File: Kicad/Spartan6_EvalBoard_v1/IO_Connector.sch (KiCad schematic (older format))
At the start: 0 parts

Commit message: Schematic almost done
Schematic almost done, just to connect connector to FPGA
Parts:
- added C? (x4): 10u, ~, symbol C
- added C? (x4): 1u, ~, symbol C
- added C? (x4): 100n, ~, symbol C
- added D?: DIODESCH, ~, symbol DIODESCH
- added J? (x2): CON2X50, MODULE, symbol CON2X50
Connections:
- net labels added: +1.2V, +3.3V, +5V, GND, IO1, IO10, IO11, IO12, IO13, IO14, IO15, IO16, IO17, IO18, IO19, IO2, IO20, IO21, IO22, IO23, IO24, IO25, IO26, IO27, IO28, IO29, IO3, IO30, IO31, IO32, IO33, IO34, IO35, IO36, IO37, IO38, IO39, IO4, IO40, IO41, IO42, IO43, IO44, IO45, IO46, IO47, IO48, IO49, IO5, IO50, IO51, IO52, IO53, IO54, IO55, IO56, IO57, IO58, IO59, IO6, IO60, IO61, IO62, IO63, IO64, IO65, IO66, IO67, IO68, IO69, IO7, IO70, IO8, IO9, VCC
- wire segments 0 -> 179

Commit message: Schematic and netllist created
The correct fpga connection to connector will have to be carried out.
Some more footprints need to be created.
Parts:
- gave numbers to parts that had none: 14
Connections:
- net labels added: 1.2V, 3.3V, 5V, IO[1..70], VCC_OUT
- net labels removed: +1.2V, +3.3V, +5V
- wire segments 179 -> 134
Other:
- moved on the sheet: C201, C202, C203, C204, C205, C206, C207, C208, C209, C210, C211, C212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

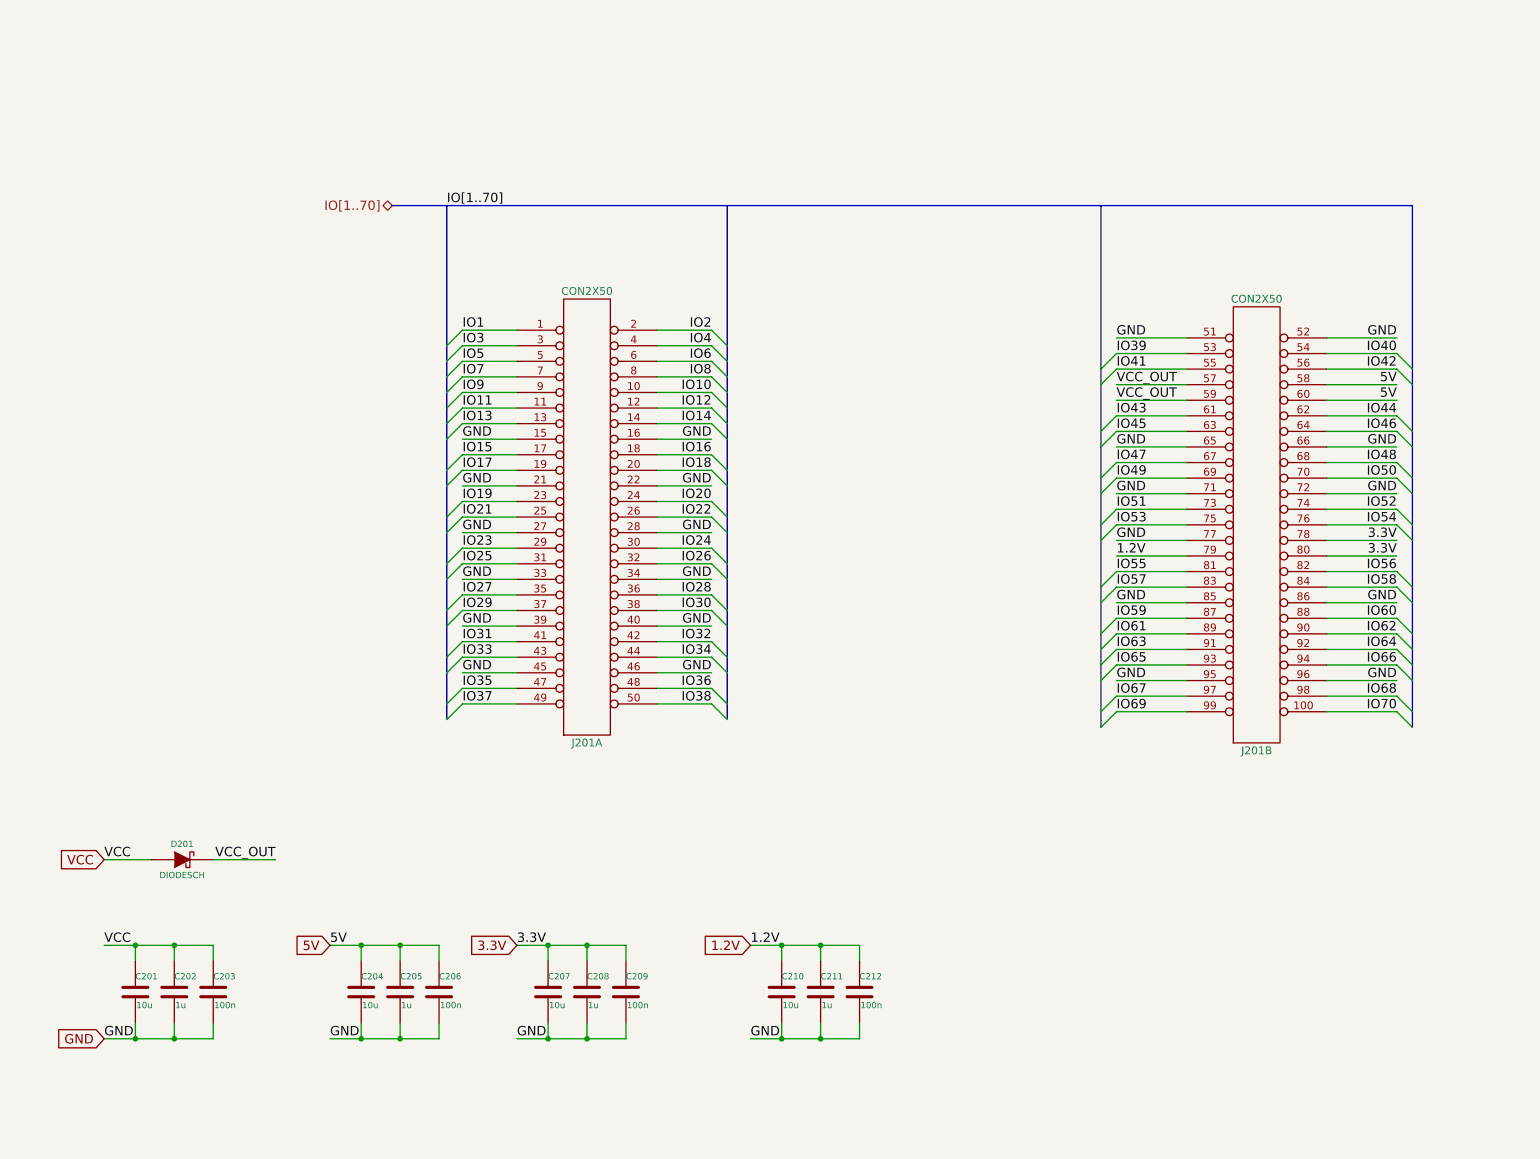
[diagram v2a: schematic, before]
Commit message: Schematic completed, layout starte
Schematic completed, layout starte
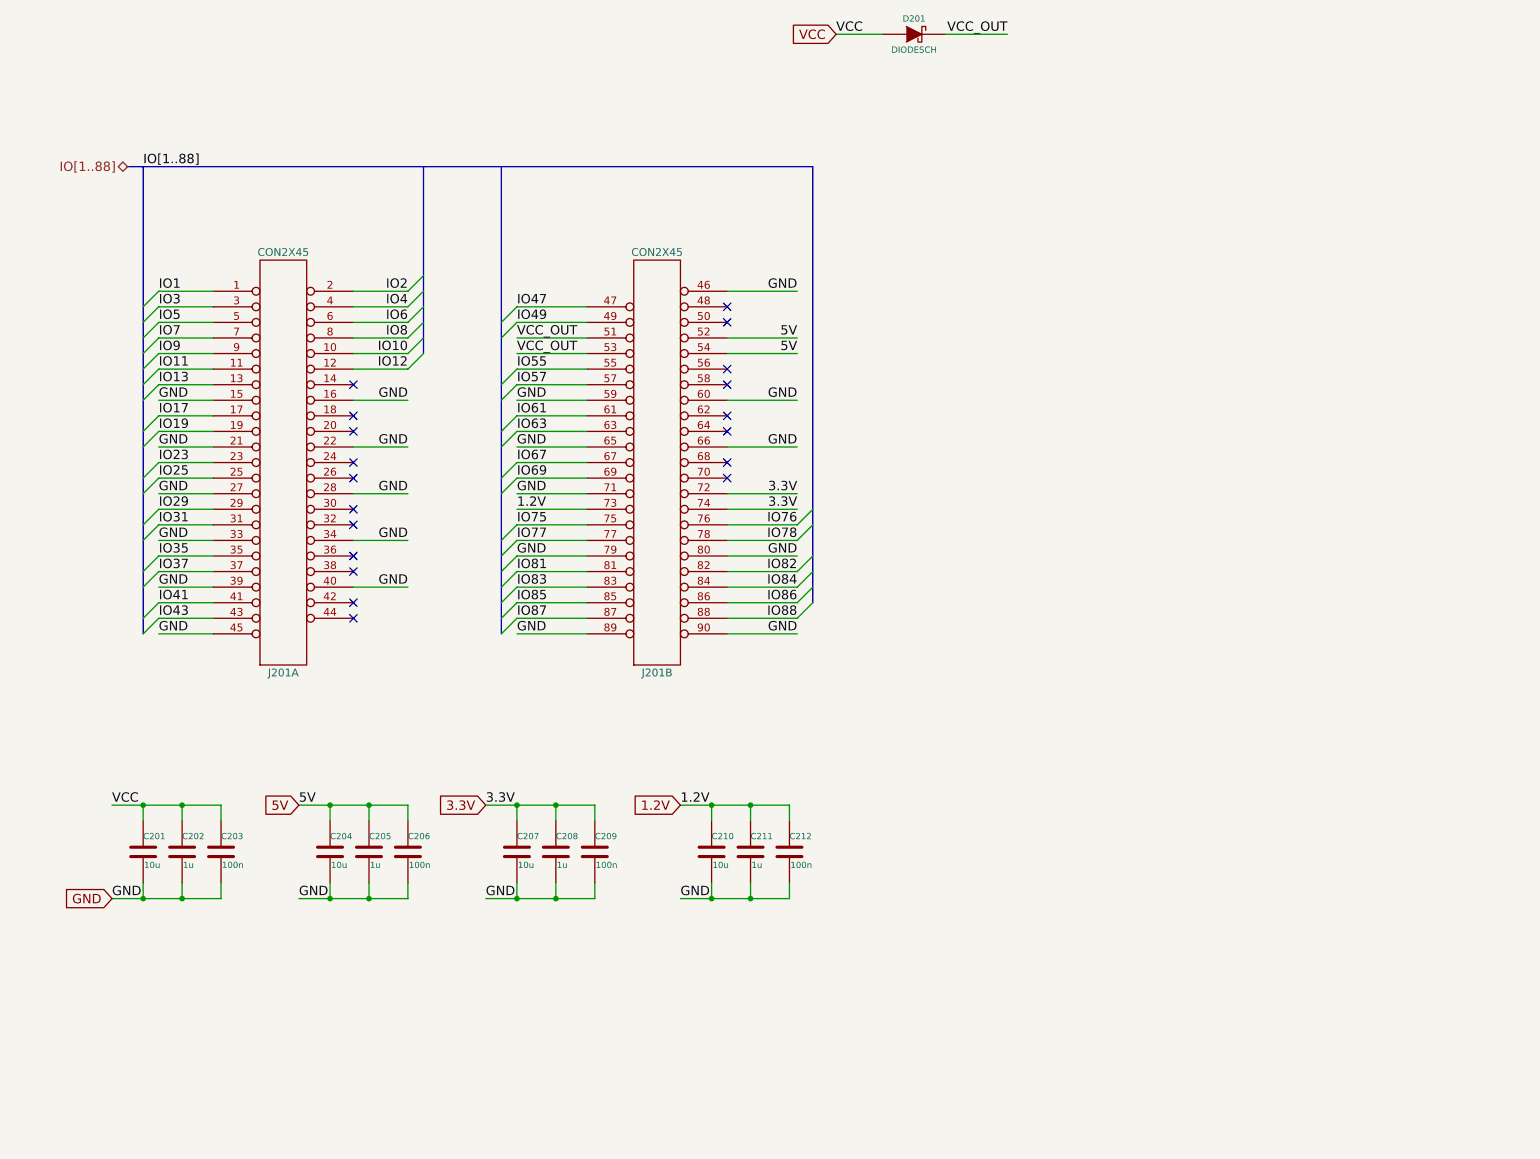
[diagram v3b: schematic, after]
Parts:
- removed J201: CON2X50, MODULE, symbol CON2X50
- added J201: CON2X45, MODULE, symbol CON2X45
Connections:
- net 1.2V: now also J201.73
- net 3.3V: now also J201.72, J201.74
- net 5V: now also J201.52, J201.54
- net GND: now also J201.15, J201.16, J201.21, J201.22, J201.27, J201.28, J201.33, J201.34, J201.39, J201.40, J201.45, J201.46, J201.59, J201.60, J201.65, J201.66, J201.71, J201.79, J201.80, J201.89, J201.90
- net IO1: now also J201.1
- net IO10: now also J201.10
- net IO11: now also J201.11
- net IO12: now also J201.12
- net IO13: now also J201.13
- net IO17: now also J201.17
- net IO19: now also J201.19
- net IO2: now also J201.2
- net IO23: now also J201.23
- net IO25: now also J201.25
- net IO29: now also J201.29
- net IO3: now also J201.3
- net IO31: now also J201.31
- net IO35: now also J201.35
- net IO37: now also J201.37
- net IO4: now also J201.4
- net IO41: now also J201.41
- net IO43: now also J201.43
- net IO47: now also J201.47
- net IO49: now also J201.49
- net IO5: now also J201.5
- net IO55: now also J201.55
- net IO57: now also J201.57
- net IO6: now also J201.6
- net IO61: now also J201.61
- net IO63: now also J201.63
- net IO67: now also J201.67
- net IO69: now also J201.69
- net IO7: now also J201.7
- net IO8: now also J201.8
- net IO9: now also J201.9
- net VCC_OUT: now also J201.51, J201.53
- new net IO75: J201.75
- new net IO76: J201.76
- new net IO77: J201.77
- new net IO78: J201.78
- new net IO81: J201.81
- new net IO82: J201.82
- new net IO83: J201.83
- new net IO84: J201.84
- new net IO85: J201.85
- new net IO86: J201.86
- new net IO87: J201.87
- new net IO88: J201.88
- no-connect marks 0 -> 19
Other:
- moved on the sheet: C201, C202, C203, C204, C205, C206, C207, C208, C209, C210, C211, C212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

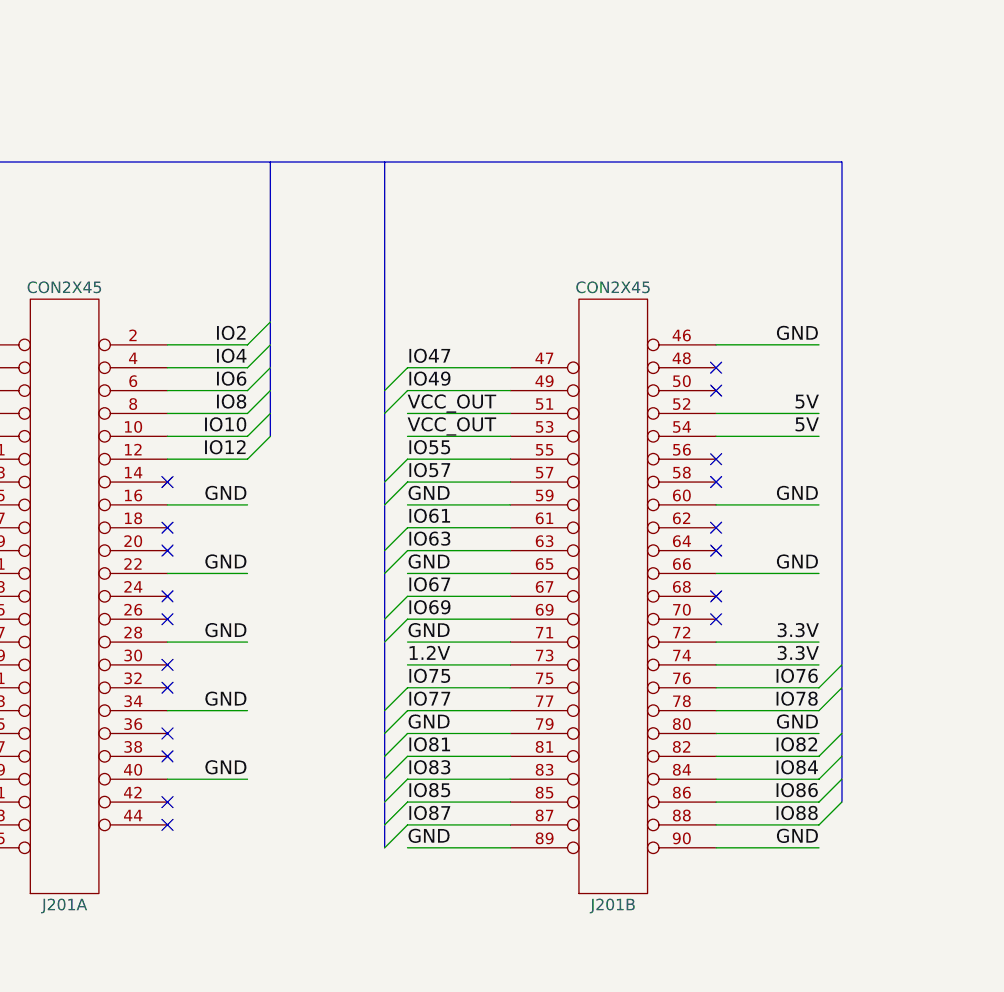
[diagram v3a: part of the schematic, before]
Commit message: BZR - Layout half done
Using LaunchPad Kicad
Layout more than half completed
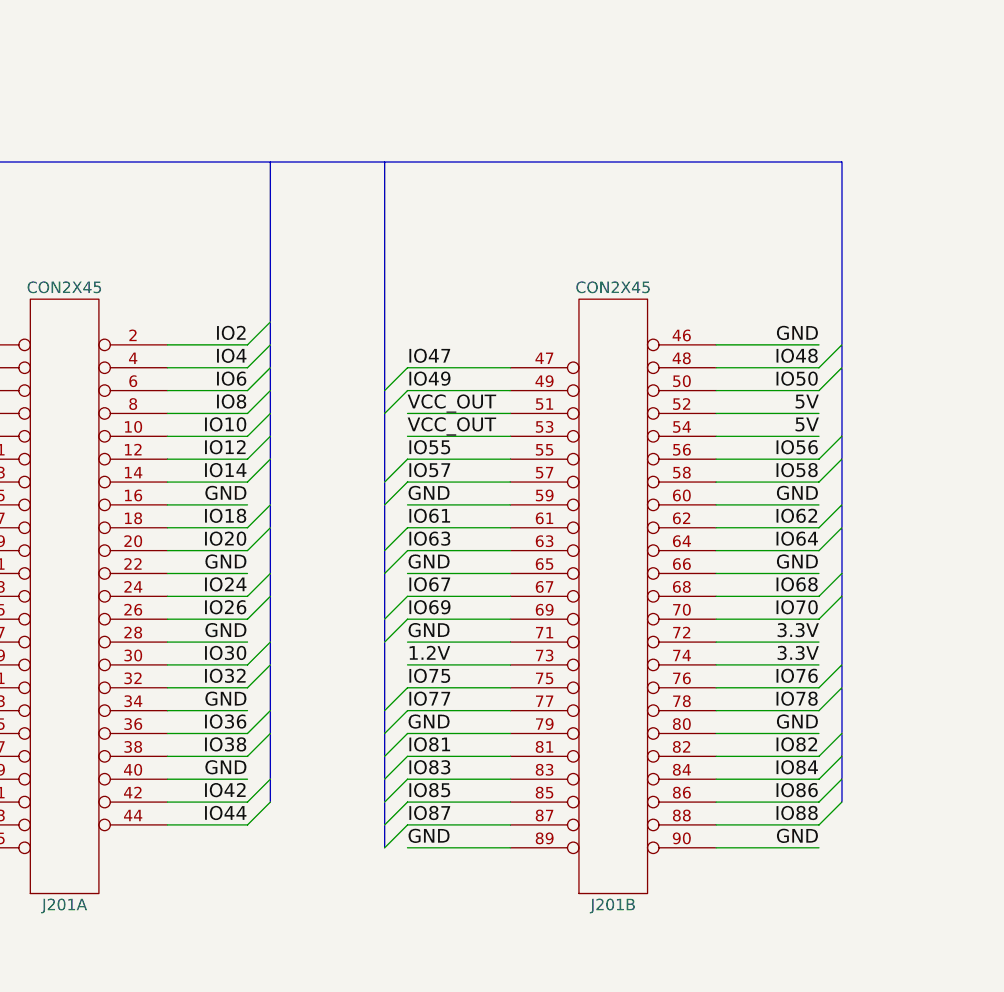
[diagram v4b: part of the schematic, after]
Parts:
- C201, C204, C207, C210: footprint ~ -> Capacitors_SMD.pretty:C_0603
- C202, C203, C205, C206, C208, C209, C211, C212: footprint ~ -> Capacitors_SMD.pretty:C_0402
- D201: footprint ~ -> Eric.mod:SOD-123FL
- J201: footprint MODULE -> Eric.mod:CON45X2
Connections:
- net IO48: now reaches J201.48
- net IO50: now reaches J201.50
- net IO56: now reaches J201.56
- net IO58: now reaches J201.58
- net IO62: now reaches J201.62
- net IO64: now reaches J201.64
- net IO68: now reaches J201.68
- net IO70: now reaches J201.70
- net IO14: now reaches J201.14
- net IO18: now reaches J201.18
- net IO20: now reaches J201.20
- net IO24: now reaches J201.24
- net IO26: now reaches J201.26
- net IO30: now reaches J201.30
- net IO32: now reaches J201.32
- net IO36: now reaches J201.36
- net IO38: now reaches J201.38
- net IO42: now reaches J201.42
- net IO44: now reaches J201.44
- no-connect marks 19 -> 0
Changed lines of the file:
@@
 LIBS:Eric
 LIBS:Spartan6_EvalBoard_v1-cache
-EELAYER 27 0
+EELAYER 25 0
 EELAYER END
 $Descr A4 11693 8268
@@
 F 0 "C201" H 1200 6450 40  0000 L CNN
 F 1 "10u" H 1206 6265 40  0000 L CNN
-F 2 "~" H 1238 6200 30  0000 C CNN
+F 2 "Capacitors_SMD.pretty:C_0603" H 1238 6200 30  0001 C CNN
 F 3 "~" H 1200 6350 60  0000 C CNN
 	1    1200 6350
@@
 F 0 "C202" H 1450 6450 40  0000 L CNN
 F 1 "1u" H 1456 6265 40  0000 L CNN
-F 2 "~" H 1488 6200 30  0000 C CNN
+F 2 "Capacitors_SMD.pretty:C_0402" H 1488 6200 30  0001 C CNN
 F 3 "~" H 1450 6350 60  0000 C CNN
 	1    1450 6350
@@
 F 0 "C203" H 1700 6450 40  0000 L CNN
 F 1 "100n" H 1706 6265 40  0000 L CNN
-F 2 "~" H 1738 6200 30  0000 C CNN
+F 2 "Capacitors_SMD.pretty:C_0402" H 1738 6200 30  0001 C CNN
 F 3 "~" H 1700 6350 60  0000 C CNN
 	1    1700 6350
@@
 F 0 "C204" H 2400 6450 40  0000 L CNN
 F 1 "10u" H 2406 6265 40  0000 L CNN
-F 2 "~" H 2438 6200 30  0000 C CNN
+F 2 "Capacitors_SMD.pretty:C_0603" H 2438 6200 30  0001 C CNN
 F 3 "~" H 2400 6350 60  0000 C CNN
 	1    2400 6350
@@
 F 0 "C205" H 2650 6450 40  0000 L CNN
 F 1 "1u" H 2656 6265 40  0000 L CNN
-F 2 "~" H 2688 6200 30  0000 C CNN
+F 2 "Capacitors_SMD.pretty:C_0402" H 2688 6200 30  0001 C CNN
 F 3 "~" H 2650 6350 60  0000 C CNN
 	1    2650 6350
@@
 F 0 "C206" H 2900 6450 40  0000 L CNN
 F 1 "100n" H 2906 6265 40  0000 L CNN
-F 2 "~" H 2938 6200 30  0000 C CNN
+F 2 "Capacitors_SMD.pretty:C_0402" H 2938 6200 30  0001 C CNN
 F 3 "~" H 2900 6350 60  0000 C CNN
 	1    2900 6350
@@
 F 0 "C207" H 3600 6450 40  0000 L CNN
 F 1 "10u" H 3606 6265 40  0000 L CNN
-F 2 "~" H 3638 6200 30  0000 C CNN
+F 2 "Capacitors_SMD.pretty:C_0603" H 3638 6200 30  0001 C CNN
 F 3 "~" H 3600 6350 60  0000 C CNN
 	1    3600 6350
@@
 F 0 "C208" H 3850 6450 40  0000 L CNN
 F 1 "1u" H 3856 6265 40  0000 L CNN
-F 2 "~" H 3888 6200 30  0000 C CNN
+F 2 "Capacitors_SMD.pretty:C_0402" H 3888 6200 30  0001 C CNN
 F 3 "~" H 3850 6350 60  0000 C CNN
 	1    3850 6350
@@
 F 0 "C209" H 4100 6450 40  0000 L CNN
 F 1 "100n" H 4106 6265 40  0000 L CNN
-F 2 "~" H 4138 6200 30  0000 C CNN
+F 2 "Capacitors_SMD.pretty:C_0402" H 4138 6200 30  0001 C CNN
 F 3 "~" H 4100 6350 60  0000 C CNN
 	1    4100 6350
@@
 F 0 "C210" H 4850 6450 40  0000 L CNN
 F 1 "10u" H 4856 6265 40  0000 L CNN
-F 2 "~" H 4888 6200 30  0000 C CNN
+F 2 "Capacitors_SMD.pretty:C_0603" H 4888 6200 30  0001 C CNN
 F 3 "~" H 4850 6350 60  0000 C CNN
 	1    4850 6350
@@
 F 0 "C211" H 5100 6450 40  0000 L CNN
 F 1 "1u" H 5106 6265 40  0000 L CNN
-F 2 "~" H 5138 6200 30  0000 C CNN
+F 2 "Capacitors_SMD.pretty:C_0402" H 5138 6200 30  0001 C CNN
 F 3 "~" H 5100 6350 60  0000 C CNN
 	1    5100 6350
@@
 F 0 "C212" H 5350 6450 40  0000 L CNN
 F 1 "100n" H 5356 6265 40  0000 L CNN
-F 2 "~" H 5388 6200 30  0000 C CNN
+F 2 "Capacitors_SMD.pretty:C_0402" H 5388 6200 30  0001 C CNN
 F 3 "~" H 5350 6350 60  0000 C CNN
 	1    5350 6350
@@
 F 0 "D201" H 6150 1200 40  0000 C CNN
 F 1 "DIODESCH" H 6150 1000 40  0000 C CNN
-F 2 "~" H 6150 1100 60  0000 C CNN
+F 2 "Eric.mod:SOD-123FL" H 6150 1100 60  0001 C CNN
 F 3 "~" H 6150 1100 60  0000 C CNN
 	1    6150 1100
@@
 Wire Wire Line
 	3600 3750 4050 3750
-NoConn ~ 4950 3550
-NoConn ~ 4950 3650
-NoConn ~ 4950 3850
-NoConn ~ 4950 3950
 Text Label 5400 3450 2    60   ~ 0
 GND
-NoConn ~ 4950 2850
-NoConn ~ 4950 2950
-NoConn ~ 4950 3250
-NoConn ~ 4950 3350
-NoConn ~ 2550 3550
-NoConn ~ 2550 3650
-NoConn ~ 2550 3850
-NoConn ~ 2550 3950
-NoConn ~ 2550 4150
-NoConn ~ 2550 4250
-NoConn ~ 2550 4450
-NoConn ~ 2550 4550
-NoConn ~ 2550 4750
-NoConn ~ 2550 4850
 $Comp
 L CON2X45 J201
@@
 F 0 "J201" H 4500 2700 50  0000 C CNN
 F 1 "CON2X45" H 4500 5400 50  0000 C CNN
-F 2 "MODULE" H 4500 2500 50  0001 C CNN
+F 2 "Eric.mod:CON45X2" H 4500 2500 50  0001 C CNN
 F 3 "DOCUMENTATION" H 4500 2600 50  0001 C CNN
 	2    4500 3950
@@
 Text Label 3600 4750 0    60   ~ 0
 IO85
-NoConn ~ 2550 3350
 Entry Wire Line
 	3500 4950 3600 4850
@@
 F 0 "J201" H 2100 2700 50  0000 C CNN
 F 1 "CON2X45" H 2100 5400 50  0000 C CNN
-F 2 "MODULE" H 2100 2500 50  0001 C CNN
+F 2 "Eric.mod:CON45X2" H 2100 2500 50  0001 C CNN
 F 3 "DOCUMENTATION" H 2100 2600 50  0001 C CNN
 	1    2100 3950
@@
 	2900 3150 3000 3050
 Wire Bus Line
-	3000 1950 3000 3150
+	3000 1950 3000 4750
 Text Label 2900 2750 2    60   ~ 0
 IO2
@@
 Text Label 5400 4250 2    60   ~ 0
 IO76
+Wire Wire Line
+	4950 3950 5400 3950
+Wire Wire Line
+	4950 3850 5400 3850
+Wire Wire Line
+	4950 3650 5400 3650
+Wire Wire Line
+	4950 3550 5400 3550
+Wire Wire Line
+	4950 3350 5400 3350
+Wire Wire Line
+	4950 3250 5400 3250
+Wire Wire Line
+	4950 2950 5400 2950
+Wire Wire Line
+	4950 2850 5400 2850
+Wire Wire Line
+	2550 3350 2900 3350
+Wire Wire Line
+	2550 3550 2900 3550
+Wire Wire Line
+	2550 3650 2900 3650
+Wire Wire Line
+	2550 3850 2900 3850
+Wire Wire Line
+	2550 3950 2900 3950
+Wire Wire Line
+	2550 4150 2900 4150
+Wire Wire Line
+	2550 4250 2900 4250
+Wire Wire Line
+	2550 4450 2900 4450
+Wire Wire Line
+	2550 4550 2900 4550
+Wire Wire Line
+	2550 4750 2900 4750
+Wire Wire Line
+	2550 4850 2900 4850
+Entry Wire Line
+	2900 4750 3000 4650
+Entry Wire Line
+	2900 4850 3000 4750
+Entry Wire Line
+	2900 4550 3000 4450
+Entry Wire Line
+	2900 4450 3000 4350
+Entry Wire Line
+	2900 4250 3000 4150
+Entry Wire Line
+	2900 4150 3000 4050
+Entry Wire Line
+	2900 3950 3000 3850
+Entry Wire Line
+	2900 3850 3000 3750
+Entry Wire Line
+	2900 3650 3000 3550
+Entry Wire Line
+	2900 3550 3000 3450
+Entry Wire Line
+	2900 3350 3000 3250
+Entry Wire Line
+	5400 3950 5500 3850
+Entry Wire Line
+	5400 3850 5500 3750
+Entry Wire Line
+	5400 3650 5500 3550
+Entry Wire Line
+	5400 3550 5500 3450
+Entry Wire Line
+	5400 3350 5500 3250
+Entry Wire Line
+	5400 3250 5500 3150
+Entry Wire Line
+	5400 2950 5500 2850
+Entry Wire Line
+	5400 2850 5500 2750
+Text Label 2900 3350 2    60   ~ 0
+IO14
+Text Label 2900 3550 2    60   ~ 0
+IO18
+Text Label 2900 3650 2    60   ~ 0
+IO20
+Text Label 2900 3850 2    60   ~ 0
+IO24
+Text Label 2900 3950 2    60   ~ 0
+IO26
+Text Label 2900 4150 2    60   ~ 0
+IO30
+Text Label 2900 4250 2    60   ~ 0
+IO32
+Text Label 2900 4450 2    60   ~ 0
+IO36
+Text Label 2900 4550 2    60   ~ 0
+IO38
+Text Label 2900 4750 2    60   ~ 0
+IO42
+Text Label 2900 4850 2    60   ~ 0
+IO44
+Text Label 5400 2850 2    60   ~ 0
+IO48
+Text Label 5400 2950 2    60   ~ 0
+IO50
+Text Label 5400 3250 2    60   ~ 0
+IO56
+Text Label 5400 3350 2    60   ~ 0
+IO58
+Text Label 5400 3550 2    60   ~ 0
+IO62
+Text Label 5400 3650 2    60   ~ 0
+IO64
+Text Label 5400 3850 2    60   ~ 0
+IO68
+Text Label 5400 3950 2    60   ~ 0
+IO70
 $EndSCHEMATC
